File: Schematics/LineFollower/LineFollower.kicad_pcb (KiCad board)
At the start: 2 copper layers, 1 part, among them U1 STM32F405VGTx

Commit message: Uploaded V1.0 of PCB
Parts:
- added C1: 100nF, Capacitor_SMD:C_0805_2012Metric_Pad1.18x1.45mm_HandSolder, F.Cu at (163.9, 128.7)
- added C10: C_Polarized_US, Capacitor_SMD:CP_Elec_4x5.3, F.Cu at (107.7, 121.7)
- added C2: 100nF, Capacitor_SMD:C_0805_2012Metric_Pad1.18x1.45mm_HandSolder, F.Cu at (112.2, 105.7)
- added C3: 100nF, Capacitor_SMD:C_0805_2012Metric_Pad1.18x1.45mm_HandSolder, F.Cu at (181.0, 65.4)
- added C4: 100nF, Capacitor_SMD:C_0805_2012Metric_Pad1.18x1.45mm_HandSolder, F.Cu at (181.0, 119.4)
- added C5: 100u, Capacitor_SMD:CP_Elec_6.3x5.4, F.Cu at (127.5, 80.7)
- added C6: 22u, Capacitor_SMD:C_0805_2012Metric_Pad1.18x1.45mm_HandSolder, F.Cu at (123.0, 70.9)
- added C7: 100n, Capacitor_SMD:C_0805_2012Metric_Pad1.18x1.45mm_HandSolder, F.Cu at (119.2, 66.0)
- added C8: 22u, Capacitor_SMD:C_0805_2012Metric_Pad1.18x1.45mm_HandSolder, F.Cu at (102.4, 66.7)
- added C9: 22u, Capacitor_SMD:C_0805_2012Metric_Pad1.18x1.45mm_HandSolder, F.Cu at (104.7, 66.7)
- added D1: WS2812B, LED_SMD:LED_WS2812B_PLCC4_5.0x5.0mm_P3.2mm, F.Cu at (183.0, 69.4)
- added D2: WS2812B, LED_SMD:LED_WS2812B_PLCC4_5.0x5.0mm_P3.2mm, F.Cu at (183.0, 115.4)
- added D3: vBatt, LED_SMD:LED_1206_3216Metric_Pad1.42x1.75mm_HandSolder, F.Cu at (98.8, 73.6)
- added D4: 3v3, LED_SMD:LED_1206_3216Metric_Pad1.42x1.75mm_HandSolder, F.Cu at (99.8, 125.4)
- added G***: LOGO, GluonLib:LogoGluon_25mm, F.Cu at (156.0, 64.4)
- added J1: Morro, Connector_FFC-FPC:TE_1-84952-0_1x10-1MP_P1.0mm_Horizontal, F.Cu at (189.9, 92.4)
- added J2: StartModule, Connector_PinHeader_2.54mm:PinHeader_1x04_P2.54mm_Vertical, F.Cu at (113.5, 122.9)
- added J3: 4en1, Connector_JST:JST_SH_SM06B-SRSS-TB_1x06-1MP_P1.00mm_Horizontal, F.Cu at (139.5, 65.1)
- added J4: UART, Connector_PinHeader_2.54mm:PinHeader_1x04_P2.54mm_Vertical, F.Cu at (106.5, 77.9)
- added JP1: BOOT_SELECT, Connector_PinHeader_2.54mm:PinHeader_1x03_P2.54mm_Vertical, F.Cu at (110.9, 77.9)
- added L1: 3u3, Inductor_SMD:L_Chilisin_BMRF00101040, F.Cu at (112.2, 66.2)
- added R1: 4k7, Resistor_SMD:R_0805_2012Metric_Pad1.20x1.40mm_HandSolder, F.Cu at (169.5, 122.9)
- added R10: 10k, Resistor_SMD:R_0805_2012Metric_Pad1.20x1.40mm_HandSolder, F.Cu at (122.4, 62.6)
- added R11: 54k9, Resistor_SMD:R_0805_2012Metric_Pad1.20x1.40mm_HandSolder, F.Cu at (122.4, 60.1)
- added R12: 4k7, Resistor_SMD:R_0805_2012Metric_Pad1.20x1.40mm_HandSolder, F.Cu at (103.7, 73.6)
- added R13: 1k, Resistor_SMD:R_0805_2012Metric_Pad1.20x1.40mm_HandSolder, F.Cu at (104.9, 125.4)
- added R2: 2k2, Resistor_SMD:R_0805_2012Metric_Pad1.20x1.40mm_HandSolder, F.Cu at (172.0, 122.9)
- added R3: 2k2, Resistor_SMD:R_0805_2012Metric_Pad1.20x1.40mm_HandSolder, F.Cu at (163.8, 131.0)
- added R4: 1k, Resistor_SMD:R_0805_2012Metric_Pad1.20x1.40mm_HandSolder, F.Cu at (174.5, 122.9)
- added R5: 10k, Resistor_SMD:R_1206_3216Metric_Pad1.30x1.75mm_HandSolder, F.Cu at (107.1, 105.7)
- added R6: 470, Resistor_SMD:R_0805_2012Metric_Pad1.20x1.40mm_HandSolder, F.Cu at (176.6, 65.4)
- added R7: 47k, Resistor_SMD:R_1206_3216Metric_Pad1.30x1.75mm_HandSolder, F.Cu at (119.5, 105.7)
- added R8: 10k, Resistor_SMD:R_1206_3216Metric_Pad1.30x1.75mm_HandSolder, F.Cu at (119.5, 108.9)
- added R9: 10k, Resistor_SMD:R_0805_2012Metric_Pad1.20x1.40mm_HandSolder, F.Cu at (125.5, 66.0)
- added REF**: KiCad-Logo2_5mm_SilkScreen, Symbol:KiCad-Logo2_5mm_SilkScreen, F.Cu at (155.5, 122.9)
- added SW1: SW_DIP_x04, Button_Switch_THT:SW_DIP_SPSTx04_Slide_9.78x12.34mm_W7.62mm_P2.54mm, F.Cu at (169.4, 134.4)
- added SW2: SW_Push, switches:SKPMANE010 _Silicone_6x6mm, F.Cu at (100.1, 105.7)
- added SW3: Push2, switches:SKPMANE010 _Silicone_6x6mm, F.Cu at (170.5, 49.9)
- added SW4: SW_Push_SPDT, switches:SS12D07VG2, F.Cu at (98.8, 113.0)
- added SW5: Start, switches:SKPMANE010 _Silicone_6x6mm, F.Cu at (170.5, 59.6)
- added U4: ~, modulos:5v-Reg, F.Cu at (117.5, 66.4)
- added U5: TPS563201, Package_TO_SOT_SMD:SOT-23-6, F.Cu at (122.4, 66.0)
- added U6: AMS1117-3.3, Package_TO_SOT_SMD:SOT-223-3_TabPin2, F.Cu at (106.5, 114.4)
- added kibuzzard-65DCBE20: G***, kibuzzard-65DCBE20, F.Cu at (119.5, 117.9)
- added kibuzzard-65DCBE24: G***, kibuzzard-65DCBE24, F.Cu at (119.5, 120.4)
- added kibuzzard-65DCBE28: G***, kibuzzard-65DCBE28, F.Cu at (119.6, 122.9)
- added kibuzzard-65DCBF71: G***, kibuzzard-65DCBF71, F.Cu at (114.0, 80.9)
- added kibuzzard-65DCBFCA: G***, kibuzzard-65DCBFCA, F.Cu at (102.5, 80.9)
- U1: value STM32F405VGTx -> ESP32-WROOM-E; footprint Package_QFP:LQFP-100_14x14mm_P0.5mm -> Espressif:ESP32-WROOM-32E
- moved U1 38.6 mm to (110.0, 92.4), turned to 90 degrees
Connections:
- U1 pad 1: unconnected-(U1-PE2-Pad1) -> GND
- U1 pad 10: Net-(U1-VSS-Pad10) -> /SCL
- U1 pad 11: unconnected-(U1-VDD-Pad11) -> /SDA
- U1 pad 12: unconnected-(U1-PH0-Pad12) -> /MOSFET_PWM
- U1 pad 13: unconnected-(U1-PH1-Pad13) -> /START
- U1 pad 15: unconnected-(U1-PC0-Pad15) -> GND
- U1 pad 2: unconnected-(U1-PE3-Pad2) -> +3V3
- U1 pad 24: unconnected-(U1-PA1-Pad24) -> Net-(U1-ADC2_CH2/GPIO2)
- U1 pad 25: unconnected-(U1-PA2-Pad25) -> /BOOT_SELECT
- U1 pad 27: Net-(U1-VSS-Pad10) -> /MOTOR_1
- U1 pad 28: unconnected-(U1-VDD-Pad28) -> /MOTOR_2
- U1 pad 29: unconnected-(U1-PA4-Pad29) -> Net-(U1-GPIO5)
- U1 pad 3: unconnected-(U1-PE4-Pad3) -> Net-(U1-EN/CHIP_PU)
- U1 pad 30: unconnected-(U1-PA5-Pad30) -> /MOTOR_3
- U1 pad 31: unconnected-(U1-PA6-Pad31) -> /MOTOR_4
- U1 pad 33: unconnected-(U1-PC4-Pad33) -> /RGB_PIN
- U1 pad 34: unconnected-(U1-PC5-Pad34) -> /UART_RX
- U1 pad 35: unconnected-(U1-PB0-Pad35) -> /UART_TX
- U1 pad 36: unconnected-(U1-PB1-Pad36) -> /ENC_1A
- U1 pad 37: unconnected-(U1-PB2-Pad37) -> /ENC_1B
- U1 pad 38: unconnected-(U1-PE7-Pad38) -> GND
- U1 pad 39: unconnected-(U1-PE8-Pad39) -> GND
- U1 pad 4: unconnected-(U1-PE5-Pad4) -> /V_BATT_SENSE
- U1 pad 5: unconnected-(U1-PE6-Pad5) -> /CONFIG
- U1 pad 6: unconnected-(U1-VBAT-Pad6) -> /ENC_2A
- U1 pad 7: unconnected-(U1-PC13-Pad7) -> /ENC_2B
- U1 pad 8: unconnected-(U1-PC14-Pad8) -> /V1
- U1 pad 9: unconnected-(U1-PC15-Pad9) -> /V2
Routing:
- net +3V3: track 0.00 -> 182.5 mm, vias 0 -> 4
- net +5V: track 0.00 -> 177.2 mm, vias 0 -> 4
- net /V_BATT: track 0.00 -> 95.0 mm
- net /V2: track 0.00 -> 87.2 mm, vias 0 -> 2
- net /V1: track 0.00 -> 87.2 mm, vias 0 -> 2
- net /SCL: track 0.00 -> 86.2 mm, vias 0 -> 2
- net /SDA: track 0.00 -> 86.2 mm, vias 0 -> 2
- net /CONFIG: track 0.00 -> 85.5 mm, vias 0 -> 2
- net /MOSFET_PWM: track 0.00 -> 84.3 mm, vias 0 -> 2
- net /RGB_PIN: track 0.00 -> 79.2 mm, vias 0 -> 2
- net Net-(U1-GPIO5): track 0.00 -> 72.8 mm, vias 0 -> 2
- net Net-(U1-ADC2_CH2/GPIO2): track 0.00 -> 63.8 mm, vias 0 -> 2
- net Net-(D1-DOUT): track 0.00 -> 44.7 mm, vias 0 -> 2
- net GND: track 0.00 -> 36.8 mm
- net /MOTOR_4: track 0.00 -> 34.4 mm, vias 0 -> 2
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- added copper zone on F.Cu, net +5V
- added copper zone on B.Cu, net GND
- added copper zone on F.Cu, net GND
- added copper zone on B.Cu, net Net-(U5-SW)
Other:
- board outline added: 100 x 100 mm
- board text added: "Gracias a: spuertes araba_st andygm_ zurano_ carlosbetdev 56knews gorn6_ david_wiki humiltat pipermind txusev supersonic2510 raupulus sergivv gordon_clark enlopa devjoseantonio bern245 alnaumiwebs blacai mikalet_ rafaromevi dhontecillas adiiran dcorraliza dielek arminio_ movich4 diegomallo sistemasitpro kerneltron patoovf dragore76 teoreding bark12 andrewsc08 siodh 20_leunam elchulodelanieve hack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"
- board text added: "Marrajo V1.0"
- board text added: "www.twitch.tv/labgluon"

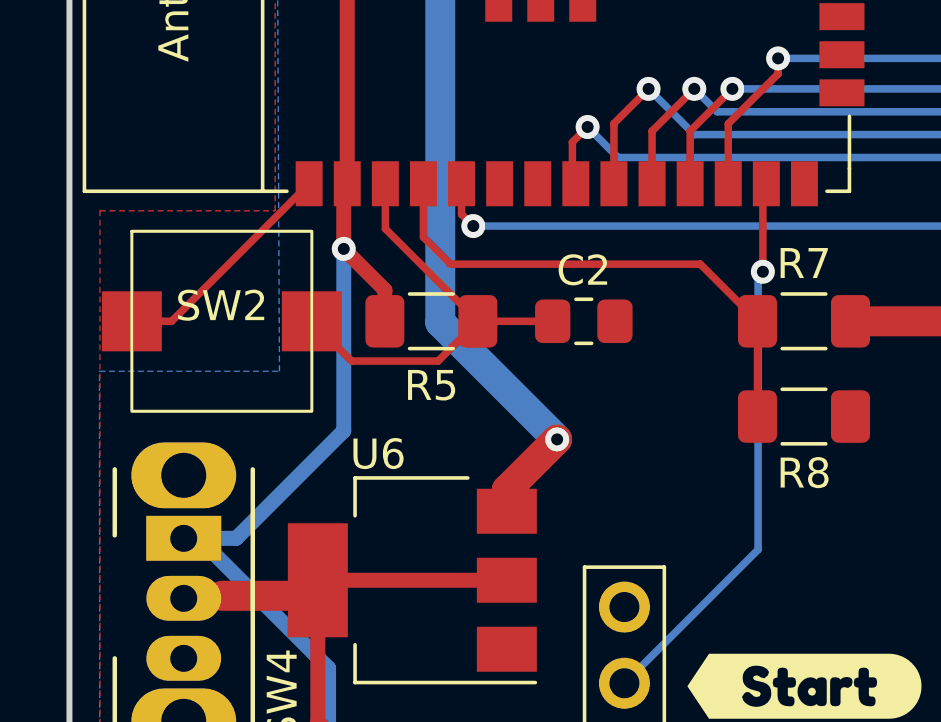
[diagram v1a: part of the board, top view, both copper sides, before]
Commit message: Version 1.1 PCB: Fixed I2C pullups
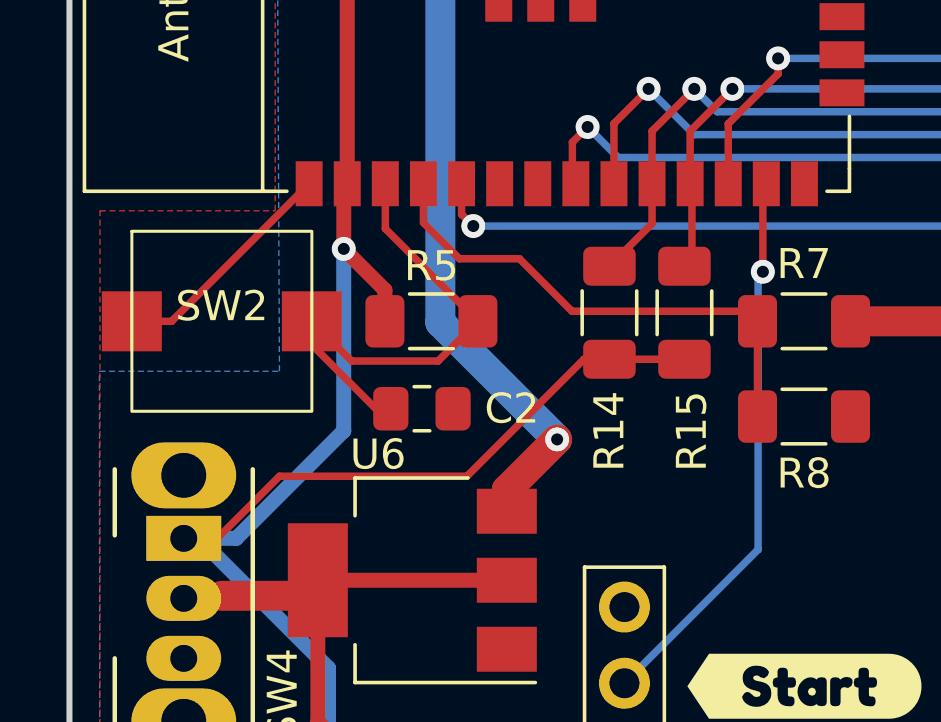
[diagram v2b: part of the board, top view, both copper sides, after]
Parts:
- added R14: 2k, Resistor_SMD:R_1206_3216Metric_Pad1.30x1.75mm_HandSolder, F.Cu at (113.0, 105.5)
- added R15: 2k, Resistor_SMD:R_1206_3216Metric_Pad1.30x1.75mm_HandSolder, F.Cu at (115.5, 105.5)
- moved C2 6.13 mm to (106.8, 108.7)
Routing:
- net +3V3: track 182.5 -> 201.6 mm
- net /SCL: track 86.2 -> 89.6 mm
- net /SDA: track 86.2 -> 89.1 mm
- net Net-(U1-EN/CHIP_PU): track 15.0 -> 16.8 mm
